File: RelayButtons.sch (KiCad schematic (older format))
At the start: 15 parts, among them J2 Screw_Terminal_01x02, K2 FTR-K3AB005W, U1 LPC54616J512, U7 KeyMatrix, U8 ULN2003ADRG3

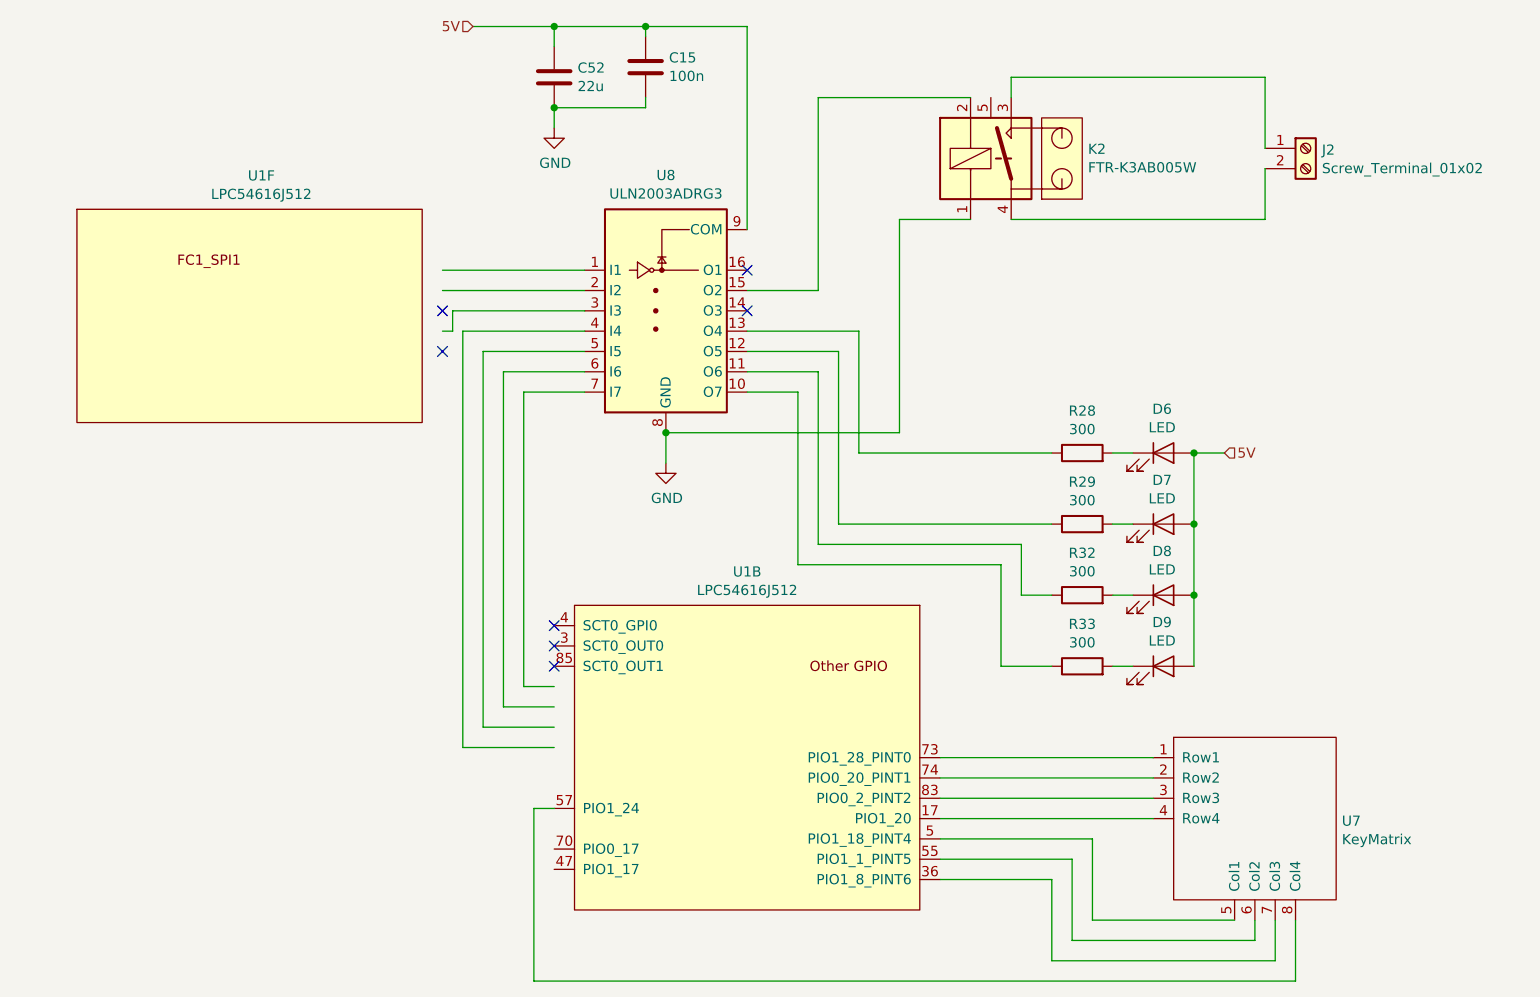
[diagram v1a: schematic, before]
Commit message: V3 bigger board, RMII instrumentation, inverter
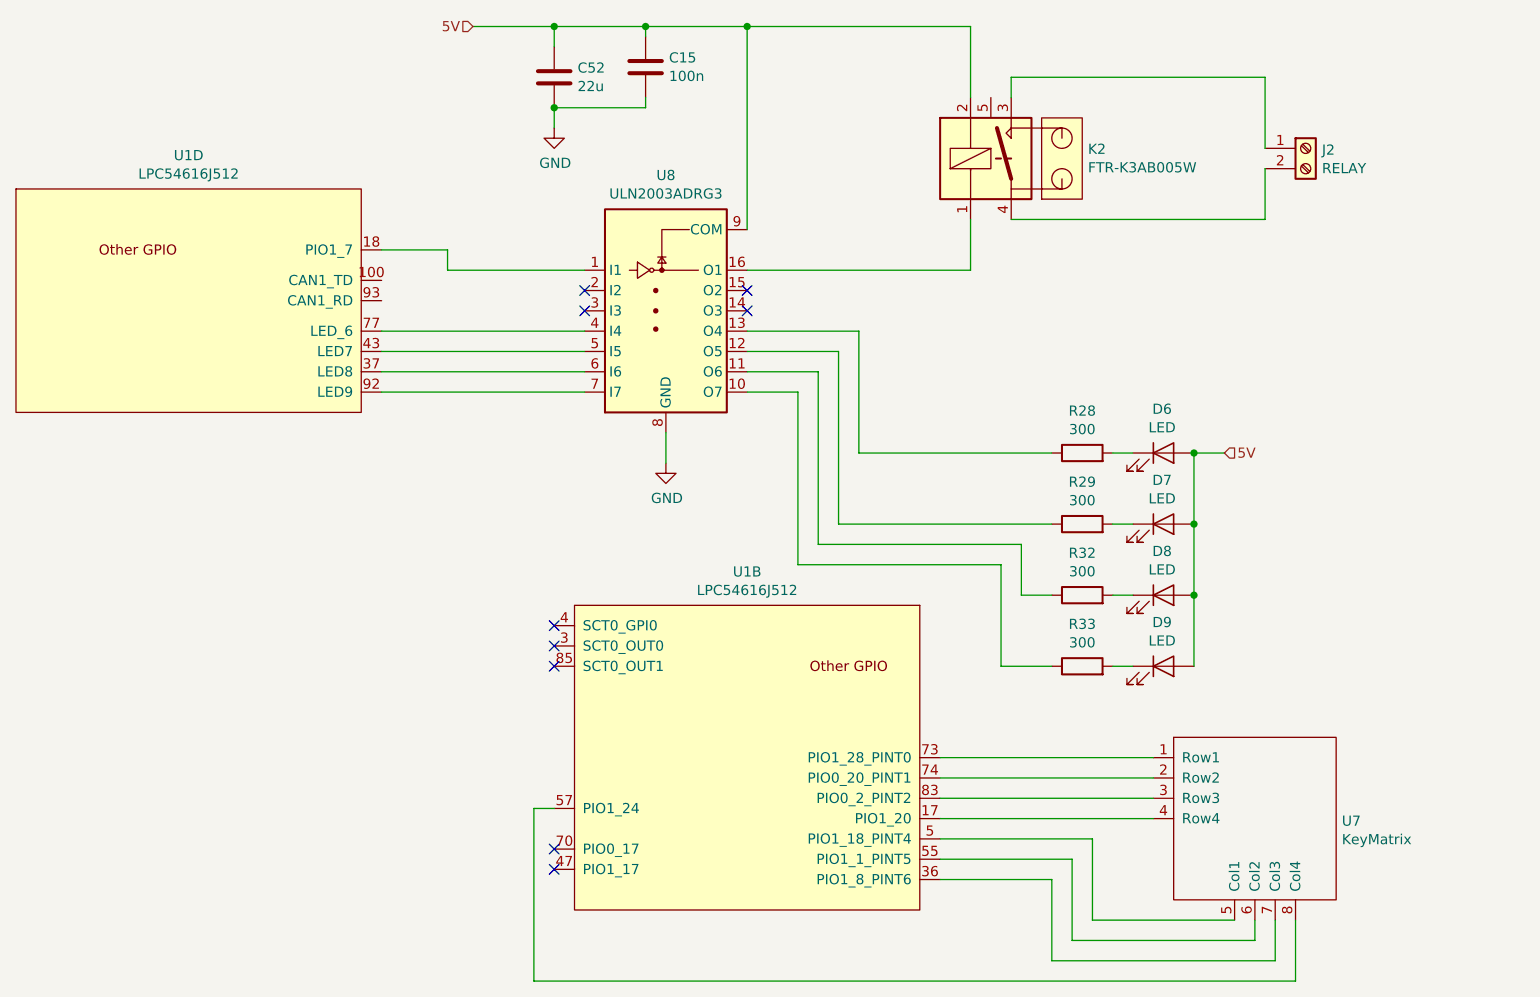
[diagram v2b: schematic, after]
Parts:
- removed unit 6 of U1
- added unit 4 of U1
- C15: JLC (none) -> C49678; OP C0805C103K1RACTU -> CC0805KRX7R9BB104
- C52: JLC (none) -> C45783
- D6, D7, D8, D9: footprint LED_THT:LED_D3.0mm -> LED_SMD:LED_1210_3225Metric; JLC (none) -> C2297
- J2: value Screw_Terminal_01x02 -> RELAY
- R28, R29, R32, R33: JLC (none) -> C17661; OP (none) -> 0805W8F3001T5E
- U8: JLC (none) -> C7512
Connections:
- wire segments 81 -> 69
- no-connect marks 7 -> 9
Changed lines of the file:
@@
-EESchema Schematic File Version 4
+EESchema Schematic File Version 5
 LIBS:canbox-cache
-EELAYER 29 0
+EELAYER 30 0
 EELAYER END
 $Descr A4 11693 8268
@@
 Comment3 ""
 Comment4 ""
+Comment5 ""
+Comment6 ""
+Comment7 ""
+Comment8 ""
+Comment9 ""
 $EndDescr
-$Comp
-L canbox-rescue:Fujitsu_FTR-K3A-Relay K2
-U 1 1 5CA79041
-P 5900 1450
-F 0 "K2" V 5946 1072 50  0000 R CNN
-F 1 "FTR-K3AB005W" V 5855 1072 50  0000 R CNN
-F 2 "cypress:ALF1T05" H 5900 1050 50  0001 C CNN
-F 3 "file:///home/thorsten/Downloads/mech_eng_lf.pdf" H 5950 2000 50  0001 C CNN
-F 4 "ALF1T05" H 700 -1600 50  0001 C CNN "OP"
-F 5 "ALF1T05" H 0   0   50  0001 C CNN "Arrow"
-F 6 "ALF1T05" H 0   0   50  0001 C CNN "DigiKez"
-	1    5900 1450
-	0    -1   -1   0
-$EndComp
 $Comp
 L canbox-rescue:ULN2003A-Transistor_Array U8
@@
 F 6 "ULN2003ADRG3" H 0   0   50  0001 C CNN "Arrow"
 F 7 "296-27596-1-ND" H 0   0   50  0001 C CNN "DigiKez"
+F 8 "C7512" H 4200 2200 50  0001 C CNN "JLC"
 	1    4200 2200
 	1    0    0    -1
@@
 Text HLabel 3250 800  0    50   Input ~ 0
 5V
-Wire Wire Line
-	5350 2800 4200 2800
-Connection ~ 4200 2800
-Wire Wire Line
-	4200 2800 4200 2950
-Wire Wire Line
-	5700 1750 5350 1750
-Wire Wire Line
-	5700 1150 4950 1150
-Wire Wire Line
-	4950 1150 4950 2100
-Wire Wire Line
-	4950 2100 4600 2100
-$Comp
-L lpc_LPC54616J512:LPC54616J512 U1
-U 6 1 5BF5C6AF
-P 1300 1700
-F 0 "U1" H 2208 1865 50  0000 C CNN
-F 1 "LPC54616J512" H 2208 1774 50  0000 C CNN
-F 2 "Package_QFP:LQFP-100_14x14mm_P0.5mm" H 1350 1550 50  0001 C CNN
-F 3 "" H 1350 1550 50  0001 C CNN
-F 4 "LPC54616J512BD100E" H 700 -1600 50  0001 C CNN "OP"
-F 5 "nm" H 0   0   50  0001 C CNN "Arrow"
-	6    1300 1700
-	1    0    0    -1
-$EndComp
-Wire Wire Line
-	3100 2300 3150 2300
-Wire Wire Line
-	3150 2300 3150 2200
-Wire Wire Line
-	3150 2200 3800 2200
-Wire Wire Line
-	3100 2100 3800 2100
-Wire Wire Line
-	3100 2000 3800 2000
-NoConn ~ 3100 2200
-NoConn ~ 3100 2400
 Wire Wire Line
 	3250 800  3650 800
@@
 F 4 "C0805C224Z3VACTU" H 3650 1050 50  0001 C CNN "OP"
 F 5 "ali" H 0   0   50  0001 C CNN "notes"
+F 6 "C45783 " H 3650 1050 50  0001 C CNN "JLC"
 	1    3650 1050
 	1    0    0    -1
@@
 	-1   0    0    -1
 $EndComp
-Wire Wire Line
-	3650 4350 3200 4350
-Wire Wire Line
-	3650 4250 3300 4250
-Wire Wire Line
-	3400 4150 3650 4150
-Wire Wire Line
-	3650 4050 3500 4050
 Text HLabel 6950 2900 2    50   Input ~ 0
 5V
@@
 F 0 "D6" H 6643 3116 50  0000 C CNN
 F 1 "LED" H 6643 3025 50  0000 C CNN
-F 2 "LED_THT:LED_D3.0mm" H 6650 2900 50  0001 C CNN
+F 2 "LED_SMD:LED_1210_3225Metric" H 6650 2900 50  0001 C CNN
 F 3 "~" H 6650 2900 50  0001 C CNN
 F 4 "151033RS03000" H 0   0   50  0001 C CNN "OP"
+F 5 "C2297" H 6650 2900 50  0001 C CNN "JLC"
 	1    6650 2900
 	1    0    0    -1
@@
 F 0 "D7" H 6643 3466 50  0000 C CNN
 F 1 "LED" H 6643 3375 50  0000 C CNN
-F 2 "LED_THT:LED_D3.0mm" H 6650 3250 50  0001 C CNN
+F 2 "LED_SMD:LED_1210_3225Metric" H 6650 3250 50  0001 C CNN
 F 3 "~" H 6650 3250 50  0001 C CNN
 F 4 "151033RS03000" H 0   0   50  0001 C CNN "OP"
+F 5 "C2297" H 6650 3250 50  0001 C CNN "JLC"
 	1    6650 3250
 	1    0    0    -1
@@
 F 0 "D8" H 6643 3816 50  0000 C CNN
 F 1 "LED" H 6643 3725 50  0000 C CNN
-F 2 "LED_THT:LED_D3.0mm" H 6650 3600 50  0001 C CNN
+F 2 "LED_SMD:LED_1210_3225Metric" H 6650 3600 50  0001 C CNN
 F 3 "~" H 6650 3600 50  0001 C CNN
 F 4 "151033RS03000" H 0   0   50  0001 C CNN "OP"
+F 5 "C2297" H 6650 3600 50  0001 C CNN "JLC"
 	1    6650 3600
 	1    0    0    -1
@@
 $Comp
 L canbox-rescue:LED-Device D9
-U 1 1 5BF70923
+U 1 1 5DA2AD5B
 P 6650 3950
 F 0 "D9" H 6643 4166 50  0000 C CNN
 F 1 "LED" H 6643 4075 50  0000 C CNN
-F 2 "LED_THT:LED_D3.0mm" H 6650 3950 50  0001 C CNN
+F 2 "LED_SMD:LED_1210_3225Metric" H 6650 3950 50  0001 C CNN
 F 3 "~" H 6650 3950 50  0001 C CNN
 F 4 "151033RS03000" H 0   0   50  0001 C CNN "OP"
+F 5 "C2297" H 6650 3950 50  0001 C CNN "JLC"
 	1    6650 3950
 	1    0    0    -1
@@
 F 4 "ok" H 0   0   50  0001 C CNN "Mouser"
 F 5 "ok" H 0   0   50  0001 C CNN "notes"
+F 6 "C17661" H 6250 2900 50  0001 C CNN "JLC"
+F 7 "0805W8F3001T5E" H 6250 2900 50  0001 C CNN "OP"
 	1    6250 2900
 	0    -1   -1   0
@@
 F 4 "ok" H 0   0   50  0001 C CNN "Mouser"
 F 5 "ok" H 0   0   50  0001 C CNN "notes"
+F 6 "C17661" H 6250 3250 50  0001 C CNN "JLC"
+F 7 "0805W8F3001T5E" H 6250 3250 50  0001 C CNN "OP"
 	1    6250 3250
 	0    -1   -1   0
@@
 F 4 "ok" H 0   0   50  0001 C CNN "Mouser"
 F 5 "ok" H 0   0   50  0001 C CNN "notes"
+F 6 "C17661" H 6250 3600 50  0001 C CNN "JLC"
+F 7 "0805W8F3001T5E" H 6250 3600 50  0001 C CNN "OP"
 	1    6250 3600
 	0    -1   -1   0
@@
 F 4 "ok" H 0   0   50  0001 C CNN "Mouser"
 F 5 "ok" H 0   0   50  0001 C CNN "notes"
+F 6 "C17661" H 6250 3950 50  0001 C CNN "JLC"
+F 7 "0805W8F3001T5E" H 6250 3950 50  0001 C CNN "OP"
 	1    6250 3950
 	0    -1   -1   0
@@
 Wire Wire Line
 	4850 2600 4600 2600
-Wire Wire Line
-	3500 2600 3500 4050
-Wire Wire Line
-	3500 2600 3800 2600
-Wire Wire Line
-	3400 2500 3800 2500
-Wire Wire Line
-	3400 2500 3400 4150
-Wire Wire Line
-	3300 2400 3300 4250
-Wire Wire Line
-	3300 2400 3800 2400
-Wire Wire Line
-	3200 2300 3200 4350
-Wire Wire Line
-	3200 2300 3800 2300
 Wire Wire Line
 	6400 3950 6500 3950
@@
 Wire Wire Line
 	3550 4650 3650 4650
-NoConn ~ 4600 2000
-NoConn ~ 3650 3750
-NoConn ~ 3650 3850
-NoConn ~ 3650 3950
-Wire Wire Line
-	5350 1750 5350 2800
 NoConn ~ 4600 2200
 $Comp
@@
 AR Path="/5CA6EA6B/5C147E9B" Ref="J2"  Part="1"
 F 0 "J2" H 7430 1392 50  0000 L CNN
-F 1 "Screw_Terminal_01x02" H 7430 1301 50  0000 L CNN
+F 1 "RELAY" H 7430 1301 50  0000 L CNN
 F 2 "TerminalBlock_Phoenix:TerminalBlock_Phoenix_MPT-0,5-2-2.54_1x02_P2.54mm_Horizontal" H 7350 1400 50  0001 C CNN
 F 3 "~" H 7350 1400 50  0001 C CNN
@@
 F 2 "Capacitor_SMD:C_0805_2012Metric_Pad1.15x1.40mm_HandSolder" H 4138 850 50  0001 C CNN
 F 3 "~" H 4100 1000 50  0001 C CNN
-F 4 "C0805C103K1RACTU" H 4100 1000 50  0001 C CNN "OP"
+F 4 "CC0805KRX7R9BB104" H 4100 1000 50  0001 C CNN "OP"
 F 5 "ali" H 450 -50 50  0001 C CNN "notes"
+F 6 " C49678 " H 4100 1000 50  0001 C CNN "JLC"
 	1    4100 1000
 	1    0    0    -1
@@
 Wire Wire Line
 	4100 800  4600 800
+$Comp
+L canbox-rescue:Fujitsu_FTR-K3A-Relay K2
+U 1 1 5CA79041
+P 5900 1450
+F 0 "K2" V 5946 1072 50  0000 R CNN
+F 1 "FTR-K3AB005W" V 5855 1072 50  0000 R CNN
+F 2 "cypress:ALF1T05" H 5900 1050 50  0001 C CNN
+F 3 "file:///home/thorsten/Downloads/mech_eng_lf.pdf" H 5950 2000 50  0001 C CNN
+F 4 "ALF1T05" H 700 -1600 50  0001 C CNN "OP"
+F 5 "ALF1T05" H 0   0   50  0001 C CNN "Arrow"
+F 6 "ALF1T05" H 0   0   50  0001 C CNN "DigiKez"
+	1    5900 1450
+	0    -1   -1   0
+$EndComp
+NoConn ~ 3650 4950
+Wire Wire Line
+	3800 2600 2800 2600
+Wire Wire Line
+	2800 2500 3800 2500
+Wire Wire Line
+	3800 2400 2800 2400
+Wire Wire Line
+	2800 2300 3800 2300
+NoConn ~ 4600 2100
+NoConn ~ 3800 2100
+NoConn ~ 3800 2200
+NoConn ~ 3650 4850
+NoConn ~ 3650 3950
+NoConn ~ 3650 3850
+$Comp
+L lpc_LPC54616J512:LPC54616J512 U1
+U 4 1 5EC46C80
+P 1000 1600
+F 0 "U1" H 1850 1765 50  0000 C CNN
+F 1 "LPC54616J512" H 1850 1674 50  0000 C CNN
+F 2 "" H 1050 1450 50  0001 C CNN
+F 3 "" H 1050 1450 50  0001 C CNN
+F 4 "nm" H -4450 -2050 50  0001 C CNN "Arrow"
+	4    1000 1600
+	1    0    0    -1
+$EndComp
+Wire Wire Line
+	3800 2000 3125 2000
+Wire Wire Line
+	3125 2000 3125 1900
+Wire Wire Line
+	3125 1900 2800 1900
+NoConn ~ 3650 3750
+Wire Wire Line
+	4200 2800 4200 2950
+Wire Wire Line
+	5700 2000 5700 1750
+Wire Wire Line
+	4600 2000 5700 2000
+Wire Wire Line
+	4600 800  5700 800
+Wire Wire Line
+	5700 800  5700 1150
+Connection ~ 4600 800
 $EndSCHEMATC

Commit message: Switch to 4 Layer PCB as the RMII loopback doesn't work
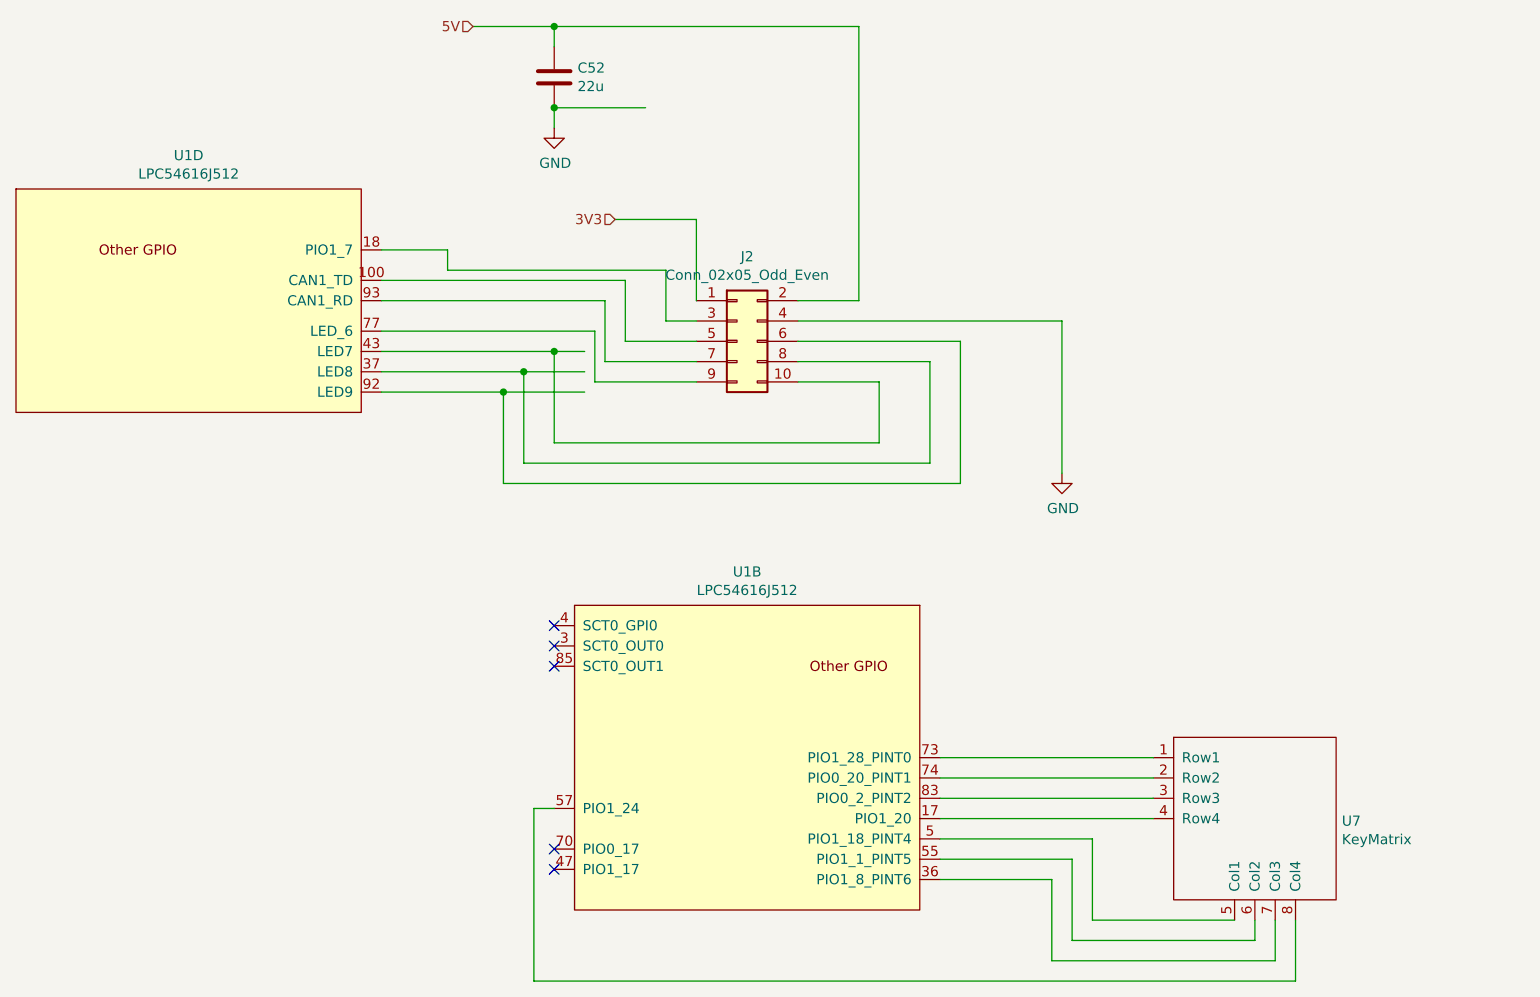
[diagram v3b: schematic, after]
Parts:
- removed C15: 100n, Capacitor_SMD:C_0805_2012Metric_Pad1.15x1.40mm_HandSolder, symbol canbox-rescue:C-Device
- removed D6, D7, D8, D9: LED, LED_SMD:LED_1210_3225Metric, symbol canbox-rescue:LED-Device
- removed J2: RELAY, TerminalBlock_Phoenix:TerminalBlock_Phoenix_MPT-0,5-2-2.54_1x02_P2.54mm_Horizontal, symbol canbox-rescue:Screw_Terminal_01x02-Connector
- removed K2: FTR-K3AB005W, cypress:ALF1T05, symbol canbox-rescue:Fujitsu_FTR-K3A-Relay
- removed R28, R29, R32, R33: 300, Resistor_SMD:R_0805_2012Metric_Pad1.15x1.40mm_HandSolder, symbol canbox-rescue:R-Device
- removed U8: ULN2003ADRG3, Package_SO:SOIC-16_3.9x9.9mm_P1.27mm, symbol canbox-rescue:ULN2003A-Transistor_Array
- added J2: Conn_02x05_Odd_Even, Connector_PinHeader_1.27mm:PinHeader_2x05_P1.27mm_Vertical_SMD, symbol Connector_Generic:Conn_02x05_Odd_Even
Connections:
- net labels added: 3V3
- wire segments 69 -> 62
- no-connect marks 9 -> 5
